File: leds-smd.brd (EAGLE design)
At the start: 100 x 75.2 mm, 66 parts

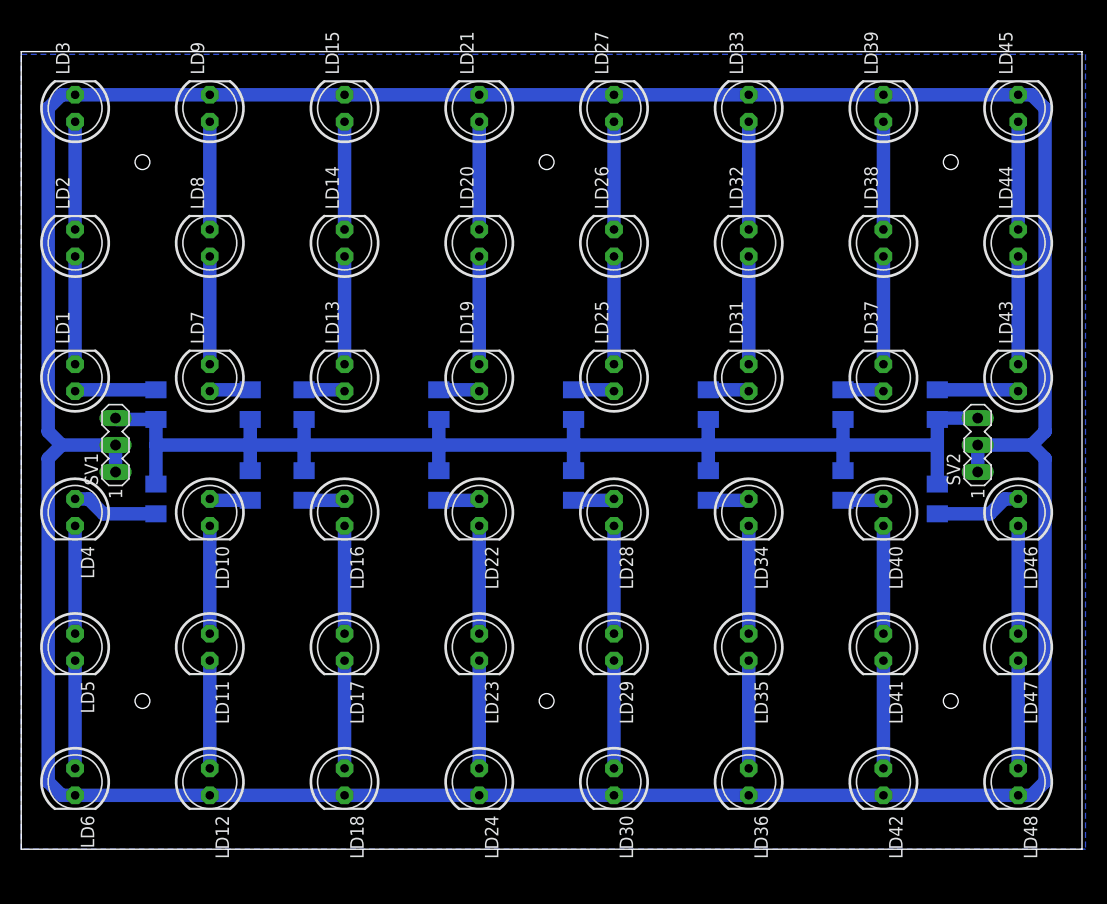
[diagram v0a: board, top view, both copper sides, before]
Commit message: Added support for 5mm leds
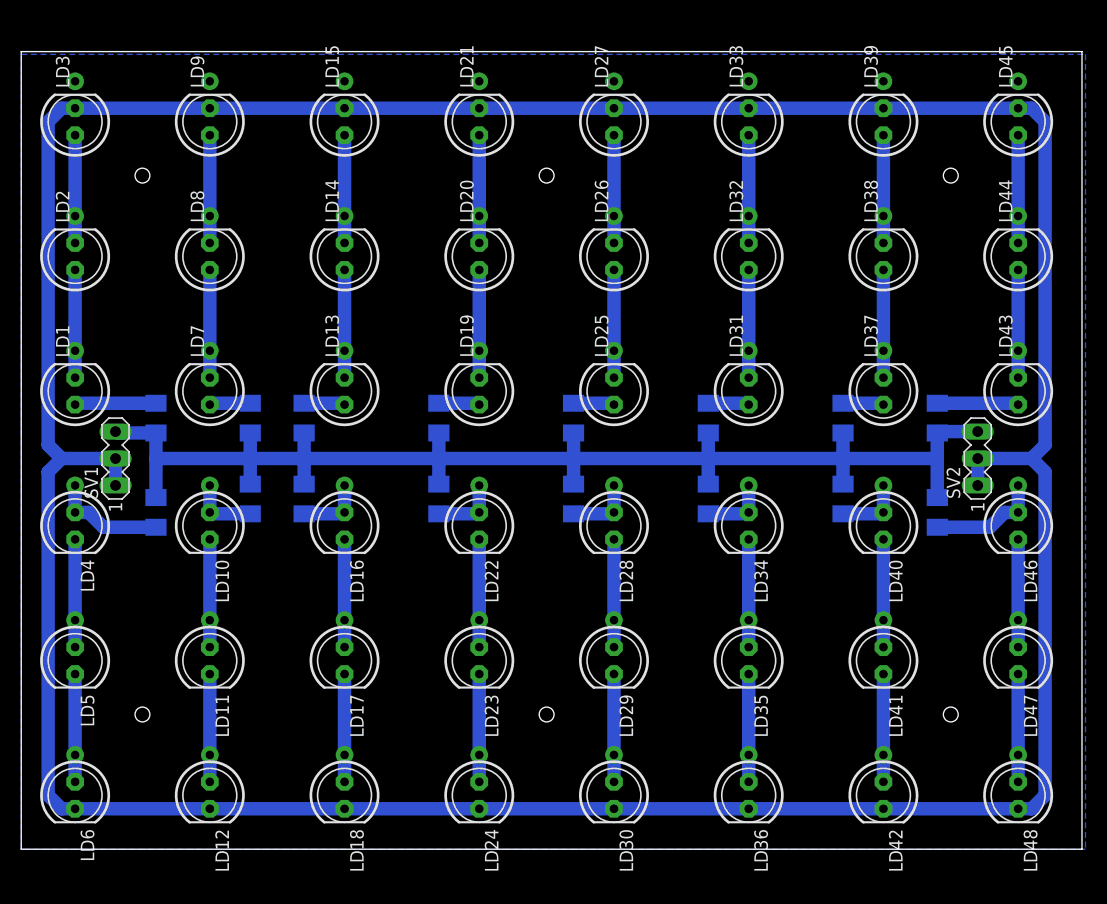
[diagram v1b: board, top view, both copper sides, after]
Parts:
- R1, R10, R11, R12, R13, R14, R15, R16, R2, R3, R4, R5, R6, R7, R8, R9: value 150 -> 120
- moved LD1 1.27 mm to (5.08, 43.2)
- moved LD13 1.27 mm to (30.5, 43.2)
- moved LD19 1.27 mm to (43.2, 43.2)
- moved LD25 1.27 mm to (55.9, 43.2)
- moved LD31 1.27 mm to (68.6, 43.2)
- moved LD37 1.27 mm to (81.3, 43.2)
- moved LD43 1.27 mm to (94.0, 43.2)
- moved LD7 1.27 mm to (17.8, 43.2)
- moved R16 1.27 mm to (86.4, 31.8)
- moved R2 1.27 mm to (12.7, 31.8)
- moved SV1 1.27 mm to (8.89, 36.8)
- moved SV2 1.27 mm to (90.2, 36.8)
- moved LD10 1.27 mm to (17.8, 30.5)
- moved LD11 1.27 mm to (17.8, 17.8)
- moved LD12 1.27 mm to (17.8, 5.08)
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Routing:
- net N$4: track 8.20 -> 10.7 mm, vias 0 -> 1
- net N$30: track 3.86 -> 6.40 mm, vias 0 -> 1
- net N$28: track 3.86 -> 6.40 mm, vias 0 -> 1
- net N$8: track 3.86 -> 6.40 mm, vias 0 -> 1
- net N$6: track 3.86 -> 6.40 mm, vias 0 -> 1
- net N$34: track 3.86 -> 6.40 mm, vias 0 -> 1
- net N$32: track 3.86 -> 6.40 mm, vias 0 -> 1
- net N$26: track 8.20 -> 10.7 mm, vias 0 -> 1
- net N$47: vias 0 -> 1
- net N$44: vias 0 -> 1
- net N$42: vias 0 -> 1
- net N$41: vias 0 -> 1
- net N$38: vias 0 -> 1
- net N$37: vias 0 -> 1
- net N$25: vias 0 -> 1
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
